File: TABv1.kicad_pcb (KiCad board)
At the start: 4 copper layers, 90 x 45 mm, 142 parts, among them IC1 TPS630702RNMR, J10 Conn_02x03_Odd_Even, J11 Conn_UART_1, J2 Conn_01x03_Socket, J3 Conn_01x03_Socket, J4 Conn_Coaxial, J5 Conn_02x06_Counter_Clockwise, J6 Conn_01x10_Socket, J7 503398-1892, J8 1053141104, J9 Conn_02x03_Odd_Even, Q1 MJD44H11T4G, Q10 PJM09P30DF, Q11 PJM09P30DF, Q12 PJM09P30DF, Q2 DMN2040U, Q3 DMN2040U, Q4 BC817-25,215, Q5 DMN2040U, Q6 DMN2040U, Q7 DMN2040U, SW1 BOOTSEL, SW2 RESET, U1 RP2350B-QFN80, U10 RAK3172, U11 LPS22DF, U2 W25Q128JVS, U4 LSM6DSV80XTR, U5 LSM6DSV80XTR, U7 LM334M, U8 LIS2MDL, U9 TESEO-LIV4F, Y1 12MHz

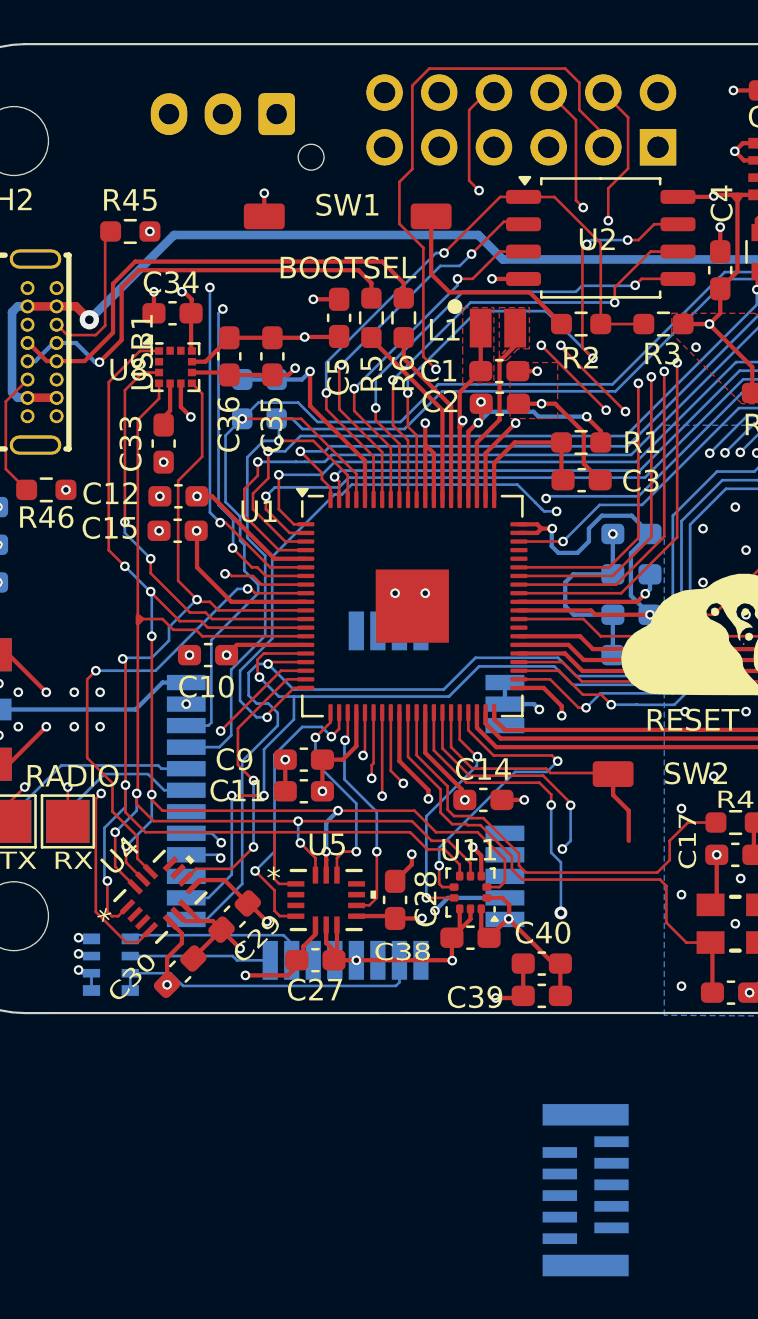
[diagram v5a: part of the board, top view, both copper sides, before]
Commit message: spostato hardware in the loop  a connettore fpc e fixata etichetta bootsel
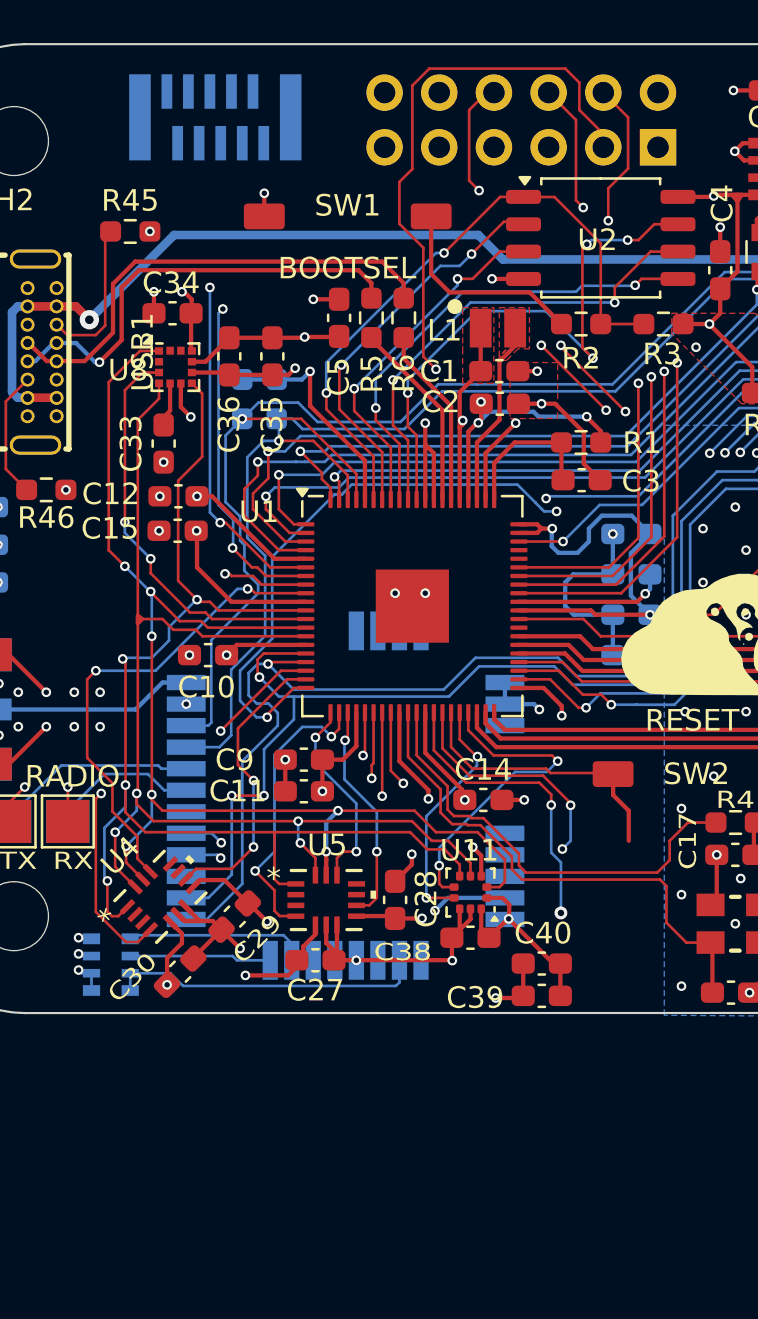
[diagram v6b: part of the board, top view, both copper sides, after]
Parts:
- removed J11: Conn_UART_1, Connector_JST:JST_XH_B3B-XH-AM_1x03_P2.50mm_Vertical
- moved J6 52.7 mm to (86.3, 36.9), turned to 180 degrees

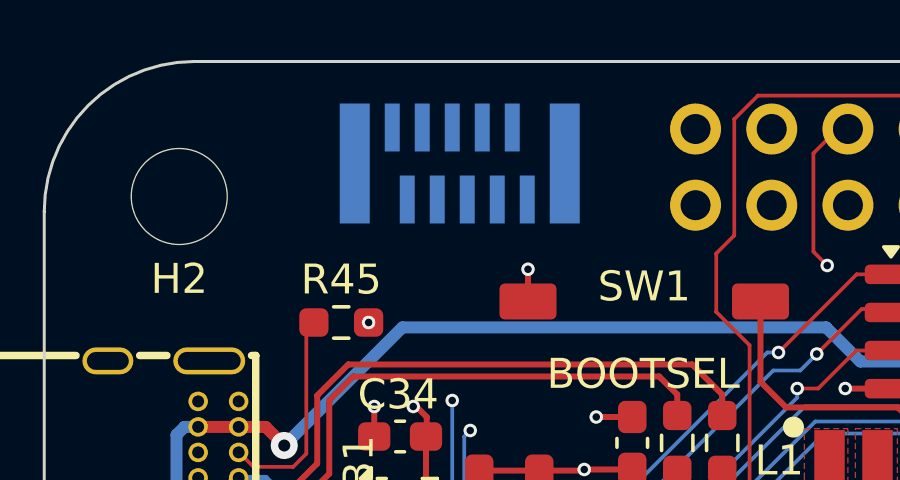
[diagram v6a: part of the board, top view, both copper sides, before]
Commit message: fpc connector update
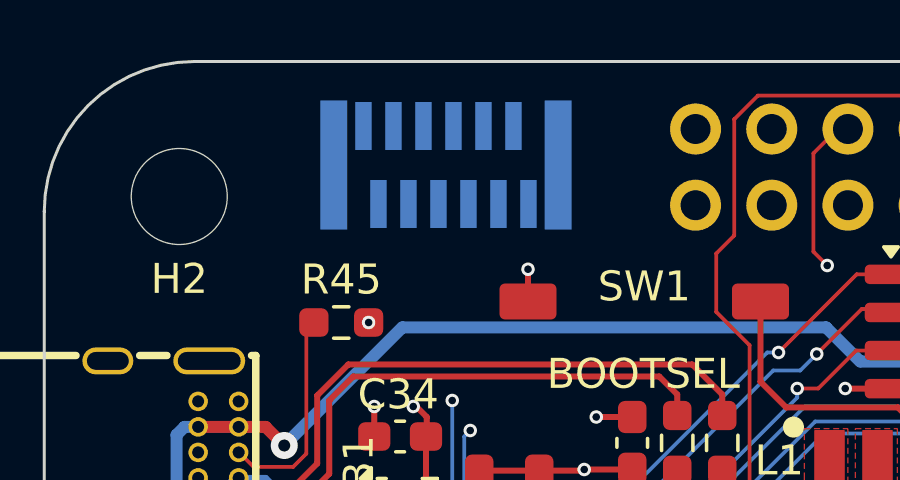
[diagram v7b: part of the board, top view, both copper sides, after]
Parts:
- removed J6: Conn_01x10_Socket, easyeda2kicad:FPC-SMD_XUNPU_FPC-0.5AD-10PB
- added FPC1: WL0540013-120R-001, easyeda2kicad:CONN-SMD_12P-WL0540013-120R-001, B.Cu at (85.9, 37.0)
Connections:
- net /QSPI Flash/~{USB_BOOT} renamed BOOTSEL
- U1 pad 6: Net-(J11-Pin_3) -> HIL_TX
- U1 pad 7: Net-(J11-Pin_2) -> HIL_RX
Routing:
- net Net-(J11-Pin_3): track 24.9 -> 0.00 mm, vias 2 -> 0
- net HIL_TX: track 0.00 -> 24.9 mm, vias 0 -> 2
- net Net-(J11-Pin_2): track 24.5 -> 0.00 mm, vias 2 -> 0
- net HIL_RX: track 0.00 -> 24.5 mm, vias 0 -> 2

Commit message: inizio rev 2.0
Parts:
- removed TP2, TP3, TP4, TP5, TP6, TP7: TestPoint_Flag, TestPoint:TestPoint_Pad_2.0x2.0mm
- removed U9: TESEO-LIV4F, TESEO_LIV4F:XCVR_TESEO-LIV4F
- added J5: Conn_02x06_Counter_Clockwise, Connector_PinHeader_2.54mm:PinHeader_2x06_P2.54mm_Vertical, B.Cu at (87.6, 47.2)
- added J5: Conn_02x06_Counter_Clockwise, Connector_PinHeader_2.54mm:PinHeader_2x06_P2.54mm_Vertical, B.Cu at (122.9, 47.2)
- ANT1, FPC1, J4, U10: moved to F.Cu
- C14: moved to B.Cu
- moved FPC1 91.6 mm to (26.7, 106.9), turned to 0 degrees
- moved ANT1 90.1 mm to (35.6, 83.7), turned to 0 degrees
- moved C39 64.9 mm to (41.0, 54.4)
- moved C40 64.9 mm to (41.0, 52.9)
- moved RN1 60.6 mm to (25.4, 53.5)
- moved J4 54.3 mm to (55.2, 115.8)
- moved LS1 51.5 mm to (85.3, 68.0), turned to 180 degrees
- moved D10 51.0 mm to (26.0, 44.4)
- moved D11 51.0 mm to (26.0, 46.2)
- moved D9 51.0 mm to (26.0, 42.7)
- moved U10 49.8 mm to (54.5, 100.8)
- moved C29 49.1 mm to (120.6, 38.0)
- moved C30 49.1 mm to (118.1, 40.6)
- moved U4 49.1 mm to (117.2, 37.1)
- moved R26 47.3 mm to (43.6, 62.6)
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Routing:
- net +3V3: track 182.8 -> 19.6 mm, vias 36 -> 7
- net GND: track 146.7 -> 35.4 mm, vias 165 -> 15
- net /PWM1: track 103.9 -> 0.00 mm, vias 4 -> 0
- net /PWM2: track 101.6 -> 0.00 mm, vias 4 -> 0
- net /PWM3: track 99.6 -> 0.00 mm, vias 2 -> 0
- net /SDA_RADIO: track 94.9 -> 0.00 mm, vias 3 -> 0
- net /PWM4: track 93.4 -> 0.00 mm, vias 2 -> 0
- net /SCL_RADIO: track 93.1 -> 0.00 mm, vias 3 -> 0
- net VUSB: track 88.8 -> 0.00 mm, vias 2 -> 0
- net /TX_GPS: track 85.9 -> 0.00 mm, vias 1 -> 0
- net /RX_GPS: track 85.0 -> 0.00 mm, vias 3 -> 0
- net +1V1: track 76.9 -> 0.00 mm, vias 4 -> 0
- net /GPIO20: track 62.7 -> 0.00 mm, vias 3 -> 0
- net /SPI1.CK: track 59.0 -> 0.00 mm, vias 7 -> 0
- net PPS: track 57.7 -> 0.00 mm, vias 1 -> 0
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- removed copper zone on F.Cu, net +3V3
- removed copper zone on B.Cu, net GND
